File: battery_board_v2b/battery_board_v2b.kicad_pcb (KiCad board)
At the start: 4 copper layers, 88 x 94.5 mm, 136 parts, among them IC1 PCA9685PW,118, IC2 LT3652IMSE#PBF, IC3 PCT2075DP,118, IC4 TPSM84209RKHT, J1 Face0, J11 CHARGE, J12 Foot0, J13 Foot1, J14 Foot2, J15 Foot3, J16 RBF, J17 BURN, J18 Bypass, J19 Heater, J2 Face1, J3 Face2, J4 Face3, J6 FC_FACE, J7 5V Breakout, J8 ISS Foot, J9 Thermocouple, K1 APAN3105, Q1 IRF7458, Q2 IRF7458, Q3 MBT2222ADW1T1, Q4 MBT2222ADW1T1, Q5 IRLML2803, Q6 NDS8434, Q7 MMBT2222AT, Q8 IRLML2803, Q9 NDS8434, U1 R5460N208AA, U10 TLVH431 DBZ SOT-23, U11 ADS1015IDGS, U2 TPS54226PWPRPWP14_2P31X2P46-L, U3 INA219AxD, U4 TCA9548APWR, U6 INA219AxD, U7 1049, U8 1049, U9 AD8495

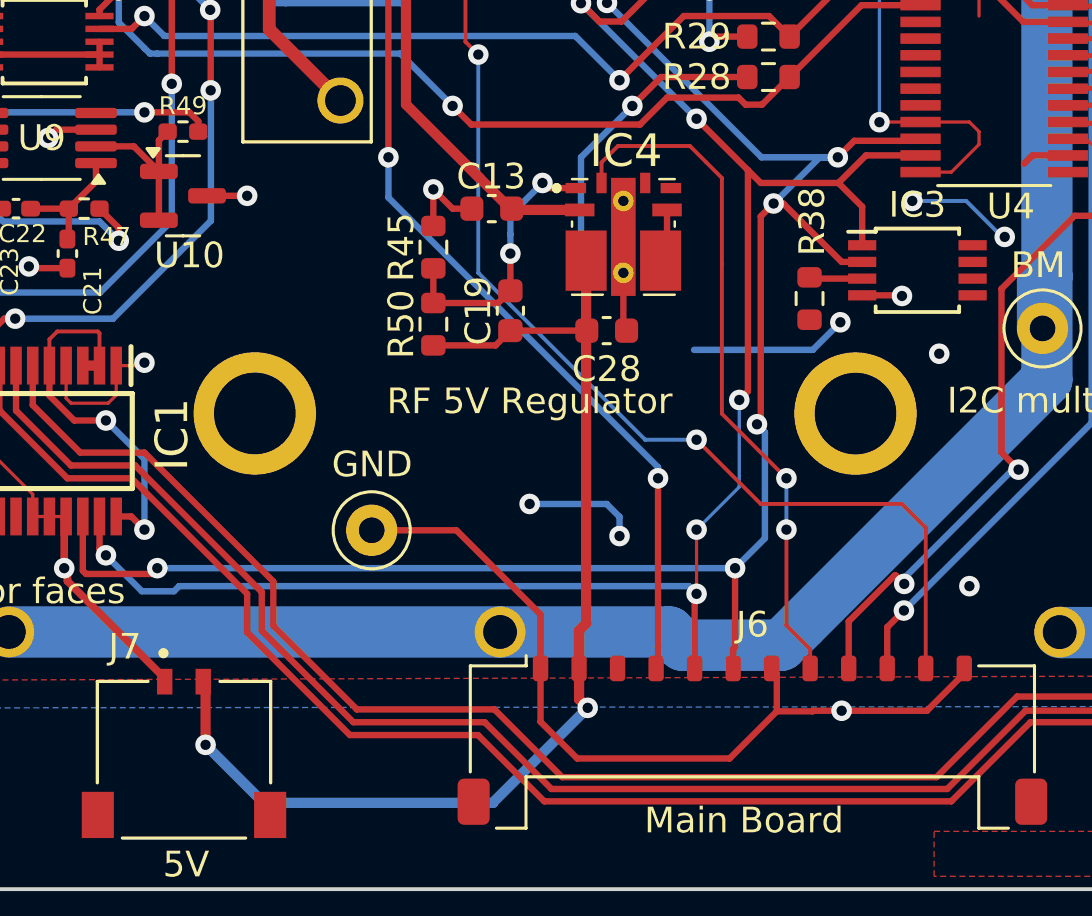
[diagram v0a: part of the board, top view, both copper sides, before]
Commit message: Changed pinout for the fc connector
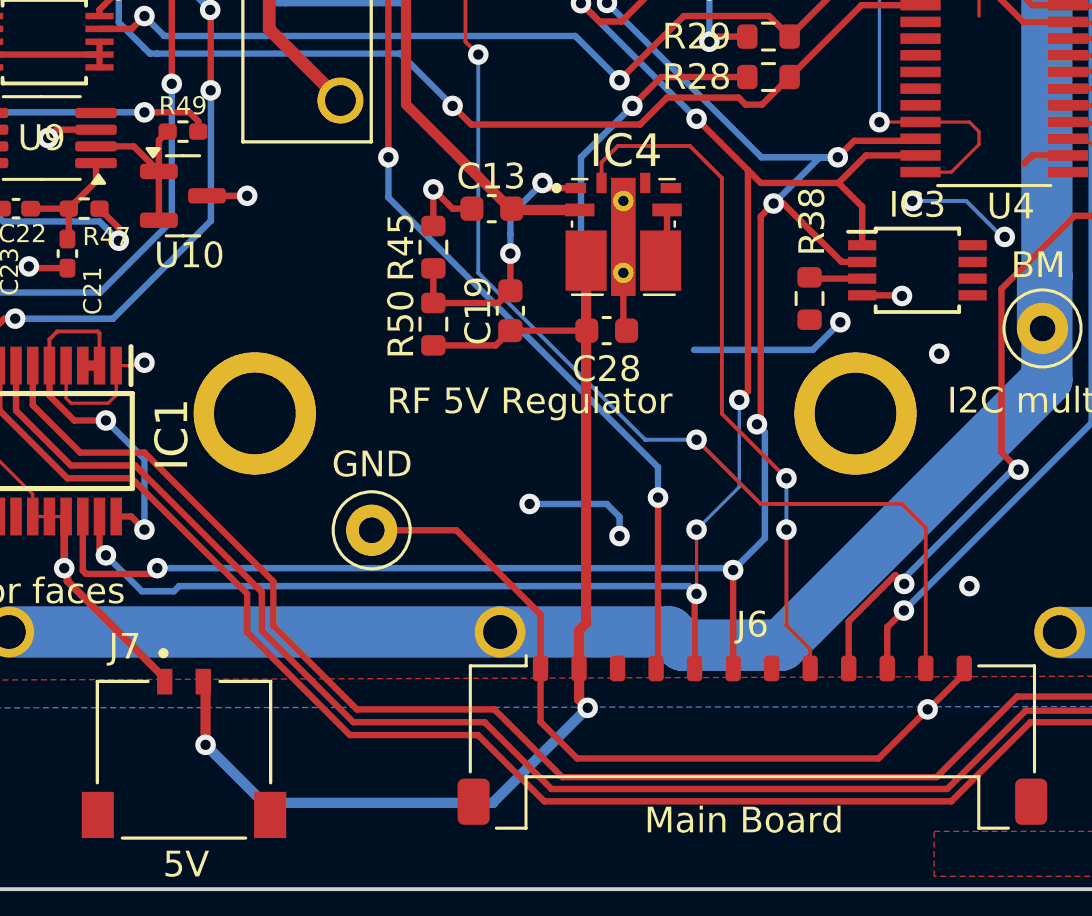
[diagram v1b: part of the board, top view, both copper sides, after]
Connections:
- J6 pad 7: GND -> +3V3
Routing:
- net GND: track 257.0 -> 255.3 mm
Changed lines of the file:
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@@
 			(layers "F.Cu" "F.Paste" "F.Mask")
 			(roundrect_rratio 0.25)
-			(net 16 "GND")
+			(net 2 "+3V3")
 			(pinfunction "Pin_7")
 			(pintype "passive")
@@
 	)
 	(segment
-		(start 145.425 124.8)
-		(end 142.15 121.525)
-		(width 0.25)
-		(layer "F.Cu")
-		(net 16)
-	)
-	(segment
 		(start 189.04 116.62)
 		(end 187.87 116.62)
@@
 	)
 	(segment
-		(start 154.625 128.575)
-		(end 154.625 127.105)
-		(width 0.25)
-		(layer "F.Cu")
-		(net 16)
-	)
-	(segment
 		(start 176.5 54.5)
 		(end 176.5 50.19)
@@
 	)
 	(segment
-		(start 142.15 121.525)
-		(end 138.85 121.525)
-		(width 0.25)
-		(layer "F.Cu")
-		(net 16)
-	)
-	(segment
 		(start 169.5784 93.1171)
 		(end 168.4504 91.9891)
@@
 	)
 	(segment
-		(start 154.625 128.575)
-		(end 152.79 130.41)
-		(width 0.25)
-		(layer "F.Cu")
-		(net 16)
-	)
-	(segment
 		(start 125.65 120.988)
 		(end 125.65 120.1235)
@@
 	)
 	(segment
-		(start 145.425 128.985)
-		(end 145.425 124.8)
-		(width 0.25)
-		(layer "F.Cu")
-		(net 16)
-	)
-	(segment
 		(start 140.502699 75.118)
 		(end 138.687098 75.118)
@@
 	)
 	(segment
+		(start 145.425 128.985)
+		(end 146.85 130.41)
+		(width 0.25)
+		(layer "F.Cu")
+		(net 16)
+	)
+	(segment
 		(start 119.67 89.5)
 		(end 122 89.5)
@@
 	)
 	(segment
-		(start 152.79 130.41)
-		(end 146.85 130.41)
-		(width 0.25)
-		(layer "F.Cu")
-		(net 16)
-	)
-	(segment
 		(start 181.506 79.5431)
 		(end 181.5568 79.4923)
@@
 	)
 	(segment
-		(start 125 98.825)
-		(end 125.575 98.25)
+		(start 146.85 130.41)
+		(end 158.59 130.41)
 		(width 0.25)
 		(layer "F.Cu")
@@
 	)
 	(segment
-		(start 156.044996 128.552502)
-		(end 156.022498 128.575)
+		(start 125 98.825)
+		(end 125.575 98.25)
 		(width 0.25)
 		(layer "F.Cu")
@@
 	)
 	(segment
+		(start 145.425 124.8)
+		(end 145.425 128.985)
+		(width 0.25)
+		(layer "F.Cu")
+		(net 16)
+	)
+	(segment
 		(start 176.649979 88.209121)
 		(end 177.95 86.9091)
@@
 	)
 	(segment
+		(start 158.59 130.41)
+		(end 160.5 128.5)
+		(width 0.25)
+		(layer "F.Cu")
+		(net 16)
+	)
+	(segment
 		(start 173 80.5)
 		(end 174 80.5)
@@
 	)
 	(segment
-		(start 157.15 128.552502)
-		(end 156.044996 128.552502)
-		(width 0.25)
-		(layer "F.Cu")
-		(net 16)
-	)
-	(segment
 		(start 128.1125 105.925)
 		(end 126.575 105.925)
@@
 	)
 	(segment
+		(start 142.15 121.525)
+		(end 145.425 124.8)
+		(width 0.25)
+		(layer "F.Cu")
+		(net 16)
+	)
+	(segment
 		(start 129.888 115.112)
 		(end 130 115)
@@
 	)
 	(segment
-		(start 156.022498 128.575)
-		(end 154.625 128.575)
-		(width 0.25)
-		(layer "F.Cu")
-		(net 16)
-	)
-	(segment
 		(start 121.4175 107.5)
 		(end 121.8 107.1175)
@@
 	)
 	(segment
-		(start 154.625 127.105)
-		(end 154.425 126.905)
-		(width 0.25)
-		(layer "F.Cu")
-		(net 16)
-	)
-	(segment
 		(start 123.95 101.5)
 		(end 123.95 100.8)
@@
 	)
 	(segment
-		(start 146.85 130.41)
-		(end 145.425 128.985)
-		(width 0.25)
-		(layer "F.Cu")
-		(net 16)
-	)
-	(segment
 		(start 159.475 112.375)
 		(end 159.5 112.4)
@@
 	)
 	(segment
-		(start 157.15 128.552502)
-		(end 160.472498 128.552502)
+		(start 138.85 121.525)
+		(end 142.15 121.525)
 		(width 0.25)
 		(layer "F.Cu")
@@
 	)
 	(via
-		(at 157.15 128.552502)
+		(at 160.5 128.5)
 		(size 0.8)
 		(drill 0.4)
@@
 	)
 	(segment
-		(start 153 126.08)
-		(end 152.925 126.155)
-		(width 0.25)
-		(layer "F.Cu")
-		(net 37)
-	)
-	(segment
 		(start 157.15 111.075)
 		(end 154.875 108.8)
@@
 	)
 	(segment
-		(start 157.641838 106.358162)
-		(end 160.141201 106.358162)
+		(start 152.925 126.905)
+		(end 152.925 123.075)
 		(width 0.25)
 		(layer "F.Cu")
@@
 	)
 	(segment
-		(start 160.141201 106.358162)
-		(end 160.221801 106.277562)
+		(start 157.641838 106.358162)
+		(end 160.141201 106.358162)
 		(width 0.25)
 		(layer "F.Cu")
@@
 	)
 	(segment
-		(start 152.925 126.155)
-		(end 152.925 126.905)
+		(start 160.141201 106.358162)
+		(end 160.221801 106.277562)
 		(width 0.25)
 		(layer "F.Cu")
@@
 	)
 	(segment
-		(start 153 126.08)
-		(end 153 123)
-		(width 0.25)
-		(layer "F.Cu")
-		(net 37)
-	)
-	(segment
 		(start 130.275 123.225)
 		(end 127.725 123.225)
@@
 	)
 	(via
-		(at 153 123)
+		(at 148.012299 100.987701)
 		(size 0.8)
 		(drill 0.4)
@@
 	)
 	(via
-		(at 148.012299 100.987701)
+		(at 152.925 123.075)
 		(size 0.8)
 		(drill 0.4)
@@
 	)
 	(segment
+		(start 152.85 123)
+		(end 152.925 123.075)
+		(width 0.25)
+		(layer "B.Cu")
+		(net 37)
+	)
+	(segment
 		(start 146.5 89.5)
 		(end 146.5 92)
@@
 	)
 	(segment
-		(start 154.163 121.837)
-		(end 153 123)
+		(start 152.925 123.075)
+		(end 154.163 121.837)
 		(width 0.25)
 		(layer "B.Cu")
@@
 	)
 	(segment
-		(start 153 123)
-		(end 130.5 123)
+		(start 130.5 123)
+		(end 152.85 123)
 		(width 0.25)
 		(layer "B.Cu")
@@
 	)
 	(segment
-		(start 150 126.83)
-		(end 149.925 126.905)
+		(start 150 121)
+		(end 150 126.08)
 		(width 0.25)
 		(layer "F.Cu")
@@
 	)
 	(segment
-		(start 142.9255 65.8969)
-		(end 140.7415 68.0809)
+		(start 150 126.83)
+		(end 149.925 126.905)
 		(width 0.25)
 		(layer "F.Cu")
@@
 	)
 	(segment
-		(start 150 119.5)
-		(end 150 126.08)
+		(start 142.9255 65.8969)
+		(end 140.7415 68.0809)
 		(width 0.25)
 		(layer "F.Cu")
@@
 	)
 	(segment
+		(start 150 121)
+		(end 150 120.25)
+		(width 0.25)
+		(layer "F.Cu")
+		(net 65)
+	)
+	(segment
 		(start 139.5 90.1145)
 		(end 139.5 107)
@@
 	)
 	(via
-		(at 150 119.5)
+		(at 150 120.25)
 		(size 0.8)
 		(drill 0.4)
@@
 	)
 	(segment
+		(start 139.5 107)
+		(end 139.5 108.567382)
+		(width 0.25)
+		(layer "B.Cu")
+		(net 65)
+	)
+	(segment
 		(start 138.5 85.5)
 		(end 138.5 85.567382)
@@
 	)
 	(segment
-		(start 150 119.5)
+		(start 139.5 108.567382)
 		(end 150 119.067382)
 		(width 0.25)
@@
 	(segment
 		(start 150 119.067382)
-		(end 139.5 108.567382)
+		(end 150 120.25)
 		(width 0.25)
 		(layer "B.Cu")
@@
 		(width 0.25)
 		(layer "B.Cu")
-		(net 65)
-	)
-	(segment
-		(start 139.5 108.567382)
-		(end 139.5 107)
-		(width 0.25)
-		(layer "B.Cu")
